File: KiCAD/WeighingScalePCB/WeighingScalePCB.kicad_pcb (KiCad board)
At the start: 4 copper layers, 83.1 x 31.9 mm, 41 parts, among them J1 Conn_01x04_Pin, Q1 MMBT2222A, Q2 BSS138, Q3 BSS138, T1 TouchPad, T2 TouchPad, U1 XIAO-ESP32-S3-SMD, U2 HX711, U3 SSD1306, U4 RT9193-33GB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

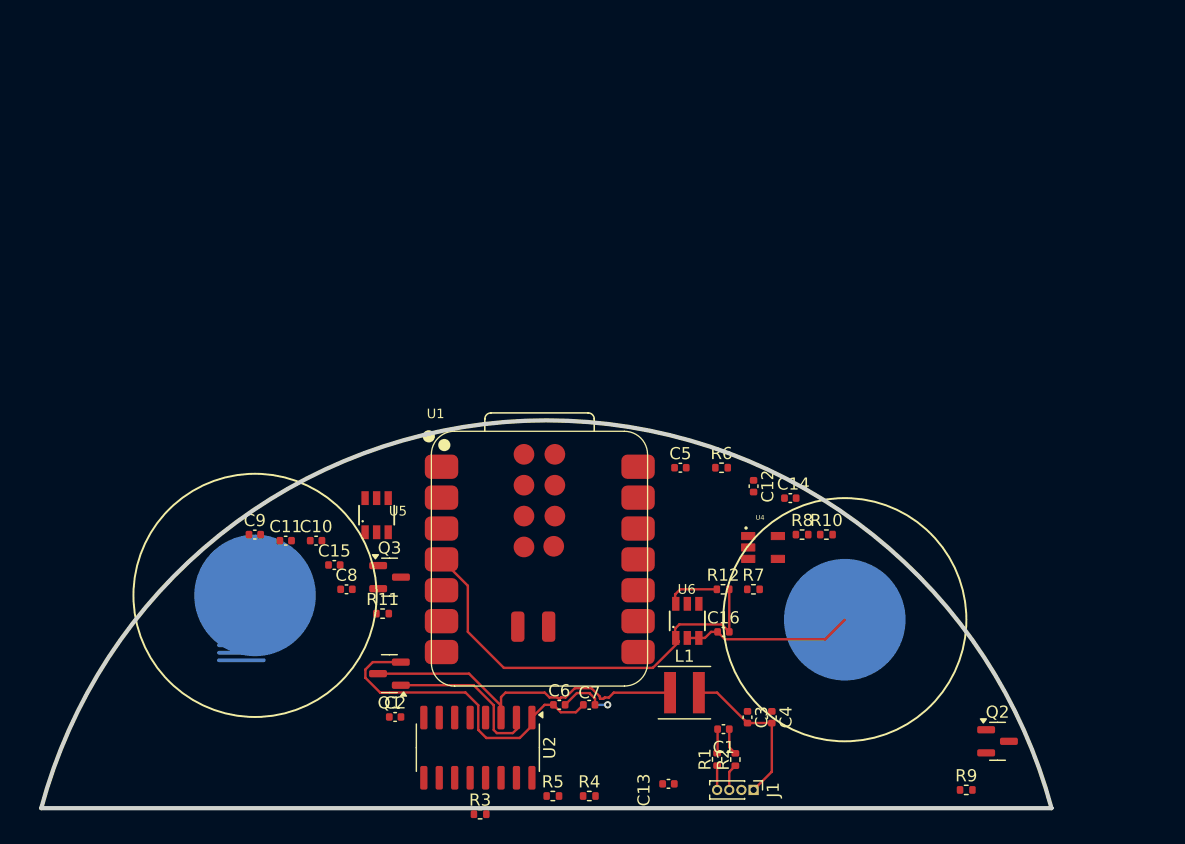
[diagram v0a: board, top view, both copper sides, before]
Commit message: imported schematic footprints to layout, noted list of missing fp
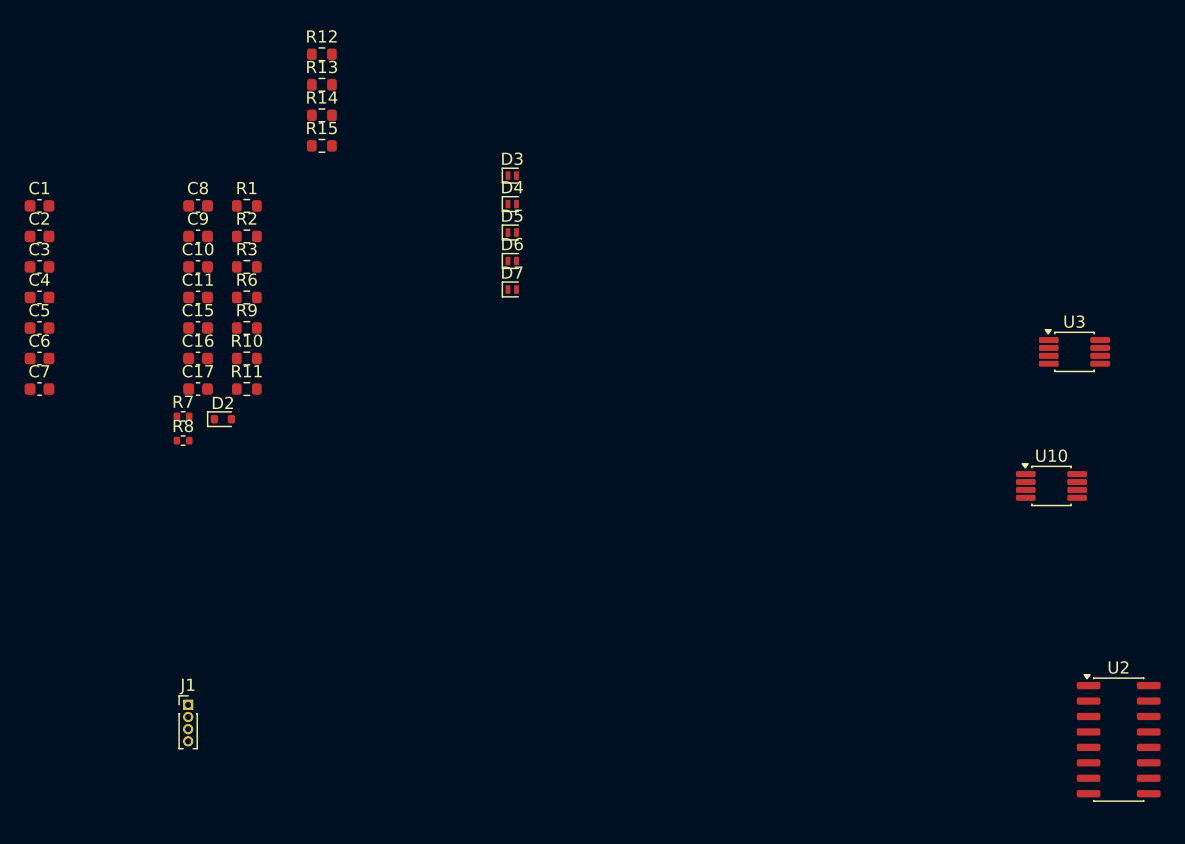
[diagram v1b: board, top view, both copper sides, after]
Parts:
- removed C12, C14: 10uF, Capacitor_SMD:C_0402_1005Metric
- removed C13: 1uF, Capacitor_SMD:C_0402_1005Metric
- removed L1: 3.3uH, Inductor_SMD:L_Coilcraft_XxL4040
- removed Q1: MMBT2222A, Package_TO_SOT_SMD:SOT-23
- removed Q2, Q3: BSS138, Package_TO_SOT_SMD:SOT-23
- removed R4, R5: 100, Resistor_SMD:R_0402_1005Metric
- removed T1, T2: TouchPad, 0my_project:Touch-Pad_10mm
- removed U1: XIAO-ESP32-S3-SMD, Seeed Studio XIAO Series Library:XIAO-ESP32C6-SMD
- removed U4: RT9193-33GB, RT9193-33GB:SOT94P279X129-5N
- removed U5, U6: TTP223-BA6, TTP223-BA6:SOT23-6
- added C17: 0.1uF, Capacitor_SMD:C_0603_1608Metric, F.Cu at (49.8, 138.5)
- added D2: 1N4148WT, Diode_SMD:D_SOD-523, F.Cu at (51.9, 141.0)
- added D3: PESD3V3U1UL, Diode_SMD:D_SOD-882, F.Cu at (75.7, 121.0)
- added D4: PESD3V3U1UL, Diode_SMD:D_SOD-882, F.Cu at (75.7, 123.3)
- added D5: PESD3V3U1UL, Diode_SMD:D_SOD-882, F.Cu at (75.7, 125.7)
- added D6: PESD3V3U1UL, Diode_SMD:D_SOD-882, F.Cu at (75.7, 128.0)
- added D7: PESD3V3U1UL, Diode_SMD:D_SOD-882, F.Cu at (75.7, 130.3)
- added R13: 10K, Resistor_SMD:R_0603_1608Metric, F.Cu at (60.0, 113.5)
- added R14: R_US, Resistor_SMD:R_0603_1608Metric, F.Cu at (60.0, 116.0)
- added R15: R_US, Resistor_SMD:R_0603_1608Metric, F.Cu at (60.0, 118.5)
- added U10: LMC555xMM, Package_SO:VSSOP-8_3x3mm_P0.65mm, F.Cu at (120.0, 146.5)
- C1, C15, C16, C2, C3, C4, C5, C6, C7: footprint Capacitor_SMD:C_0402_1005Metric -> Capacitor_SMD:C_0603_1608Metric
- C10, C8: value 1uF -> 0.1u; footprint Capacitor_SMD:C_0402_1005Metric -> Capacitor_SMD:C_0603_1608Metric
- C11: value 10uF -> 0.1u; footprint Capacitor_SMD:C_0402_1005Metric -> Capacitor_SMD:C_0603_1608Metric
- C9: value 1uF -> 1u; footprint Capacitor_SMD:C_0402_1005Metric -> Capacitor_SMD:C_0603_1608Metric
- R1, R2, R3: footprint Resistor_SMD:R_0402_1005Metric -> Resistor_SMD:R_0603_1608Metric
- R10: value 10K -> 1K; footprint Resistor_SMD:R_0402_1005Metric -> Resistor_SMD:R_0603_1608Metric
- R11: value 1K -> 200K; footprint Resistor_SMD:R_0402_1005Metric -> Resistor_SMD:R_0603_1608Metric
- R12: value 1K -> 470K; footprint Resistor_SMD:R_0402_1005Metric -> Resistor_SMD:R_0603_1608Metric
- R6: value 100 -> 200K; footprint Resistor_SMD:R_0402_1005Metric -> Resistor_SMD:R_0603_1608Metric
- R9: value 10K -> 200K; footprint Resistor_SMD:R_0402_1005Metric -> Resistor_SMD:R_0603_1608Metric
- U3: value SSD1306 -> LMC555xMM; footprint KiCad-SSD1306_OLED-0.91-128x32-master:SSD1306_OLED-0.91-128x32 -> Package_SO:VSSOP-8_3x3mm_P0.65mm; moved to F.Cu
- moved C1 70.8 mm to (36.8, 123.5), turned to 0 degrees
- moved R9 70.3 mm to (53.8, 133.5)
- moved C4 69.4 mm to (36.8, 131.0), turned to 0 degrees
- moved C3 69.0 mm to (36.8, 128.5), turned to 0 degrees
- moved R1 59.7 mm to (53.8, 123.5), turned to 0 degrees
- moved R2 58.9 mm to (53.8, 126.0), turned to 0 degrees
- moved R12 55.0 mm to (60.0, 111.0)
- moved C5 53.9 mm to (36.8, 133.5)
- moved U2 52.7 mm to (125.5, 167.4), turned to 0 degrees
- moved C7 52.1 mm to (36.8, 138.5)
- moved R8 51.5 mm to (48.6, 142.8)
- moved C6 51.4 mm to (36.8, 136.0)
- moved R10 49.8 mm to (53.8, 136.0)
- moved C2 49.2 mm to (36.8, 126.0)
- moved R7 49.0 mm to (48.6, 140.8)
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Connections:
- C10 pad 1: GND -> /trigg
- C10 pad 2: VCC -> Net-(U10-GND)
- C11 pad 1: GND -> Net-(U10-CV)
- C11 pad 2: Net-(U3-VCC) -> Net-(U10-GND)
- C8 pad 1: Net-(U3-C2N) -> Net-(U3-CV)
- C8 pad 2: Net-(U3-C2P) -> GND
- C9 pad 1: Net-(U3-C1N) -> Net-(U3-DIS)
- C9 pad 2: Net-(U3-C1P) -> GND
- R10 pad 1: VCC -> Net-(IC2-VOUT)
- R10 pad 2: SDA_5V -> GND
- R11 pad 1: VCC -> /V_BAT
- R11 pad 2: GND -> Net-(Q2-D)
- R12 pad 2: GND -> Net-(U3-DIS)
- R3 pad 1: Net-(JP1-B) -> Net-(JP3-A)
- R6 pad 1: Net-(U3-IREF) -> /V_BAT
- R6 pad 2: GND -> Net-(U1-GPIO0_A0_D0)
- R7 pad 1: 3.3V -> VCC
- R7 pad 2: SCL_3.3V -> SCL
- R8 pad 1: 3.3V -> VCC
- R8 pad 2: SDA_3.3V -> SDA
- R9 pad 1: VCC -> Net-(U1-GPIO0_A0_D0)
- R9 pad 2: SCL_5V -> GND
- U2 pad 15: Net-(JP1-B) -> Net-(JP3-B)
- U2 pad 2: Net-(Q1-B) -> unconnected-(U2-BASE-Pad2)
- U2 pad 3: Net-(Q1-C) -> Net-(J1-Pin_1)
- U2 pad 4: Net-(U2-VFB) -> GND
- U3 pad 1: Net-(U3-C2P) -> GND
- U3 pad 2: Net-(U3-C2N) -> Net-(Q4-D)
- U3 pad 3: Net-(U3-C1P) -> Net-(D5-K)
- U3 pad 4: Net-(U3-C1N) -> Net-(U3-R)
- U3 pad 5: VCC -> Net-(U3-CV)
- U3 pad 6: unconnected-(U3-NC-Pad6) -> Net-(U3-DIS)
- U3 pad 7: GND -> Net-(U3-DIS)
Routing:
- net VCC: track 31.4 -> 0.00 mm
- net Net-(Q1-C): track 29.1 -> 0.00 mm
- net Time: track 26.4 -> 0.00 mm
- net GND: track 14.7 -> 0.00 mm
- net Net-(D4-K): track 14.1 -> 0.00 mm
- net Net-(Q1-B): track 13.4 -> 0.00 mm
- net Net-(J1-Pin_1): track 13.2 -> 0.00 mm
- net Net-(U2-INA+): track 2.20 -> 0.00 mm
- net Net-(J1-Pin_3): track 2.20 -> 0.00 mm
- net Net-(U2-INA-): track 2.00 -> 0.00 mm
- net (no net): track 1.00 -> 0.00 mm, vias 1 -> 0
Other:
- board outline removed

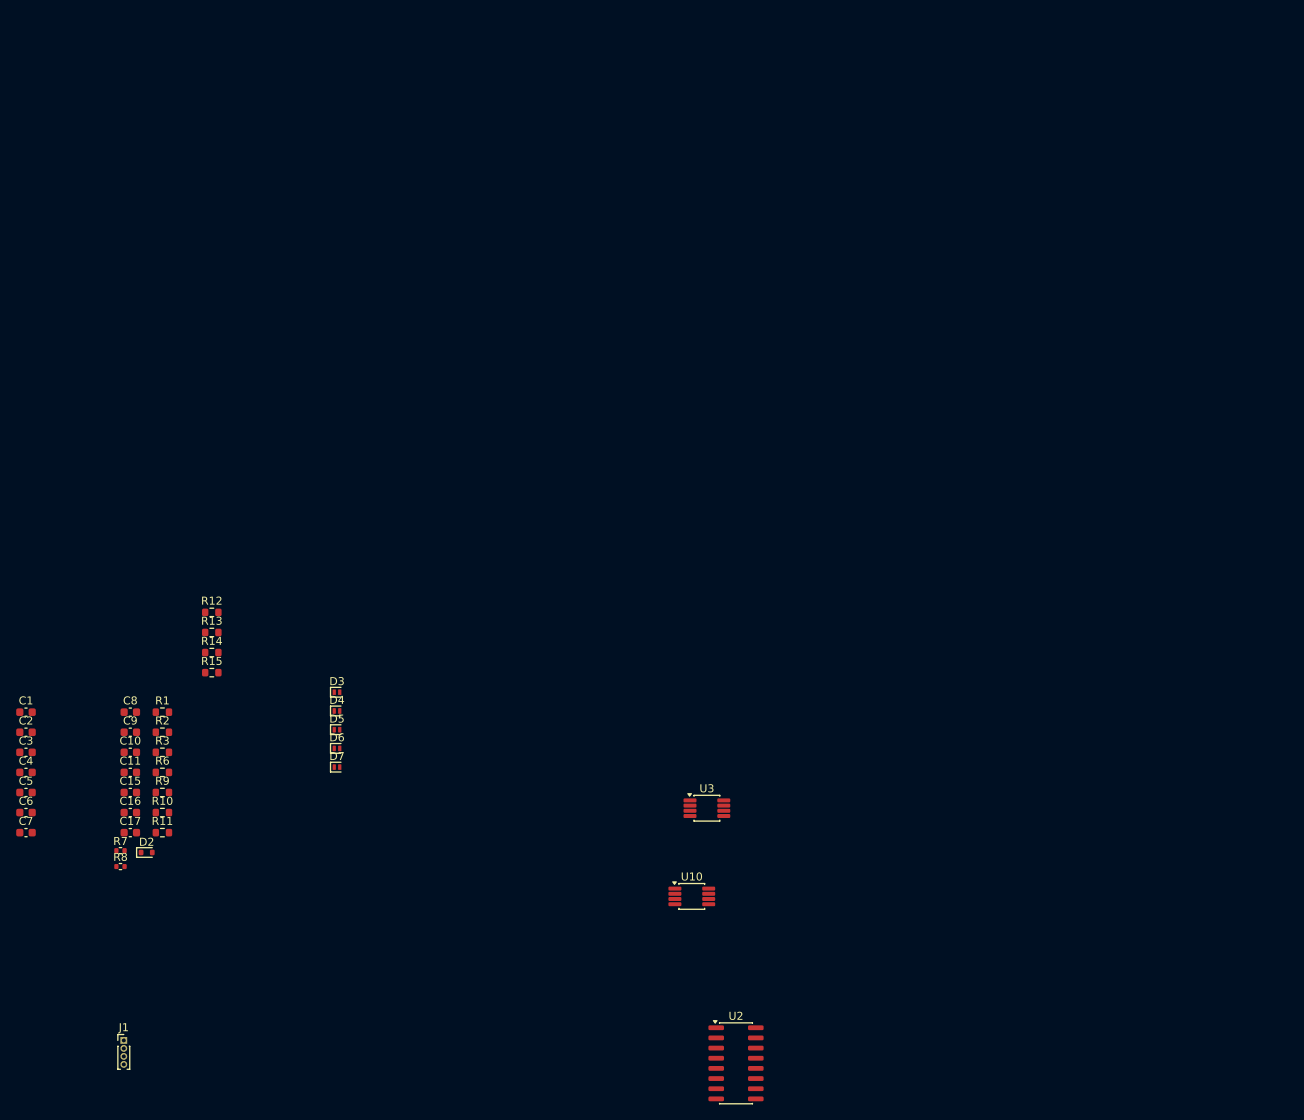
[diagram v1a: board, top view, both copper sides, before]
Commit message: Added flowchart for board and dxf in the layout for card edge and placement of components
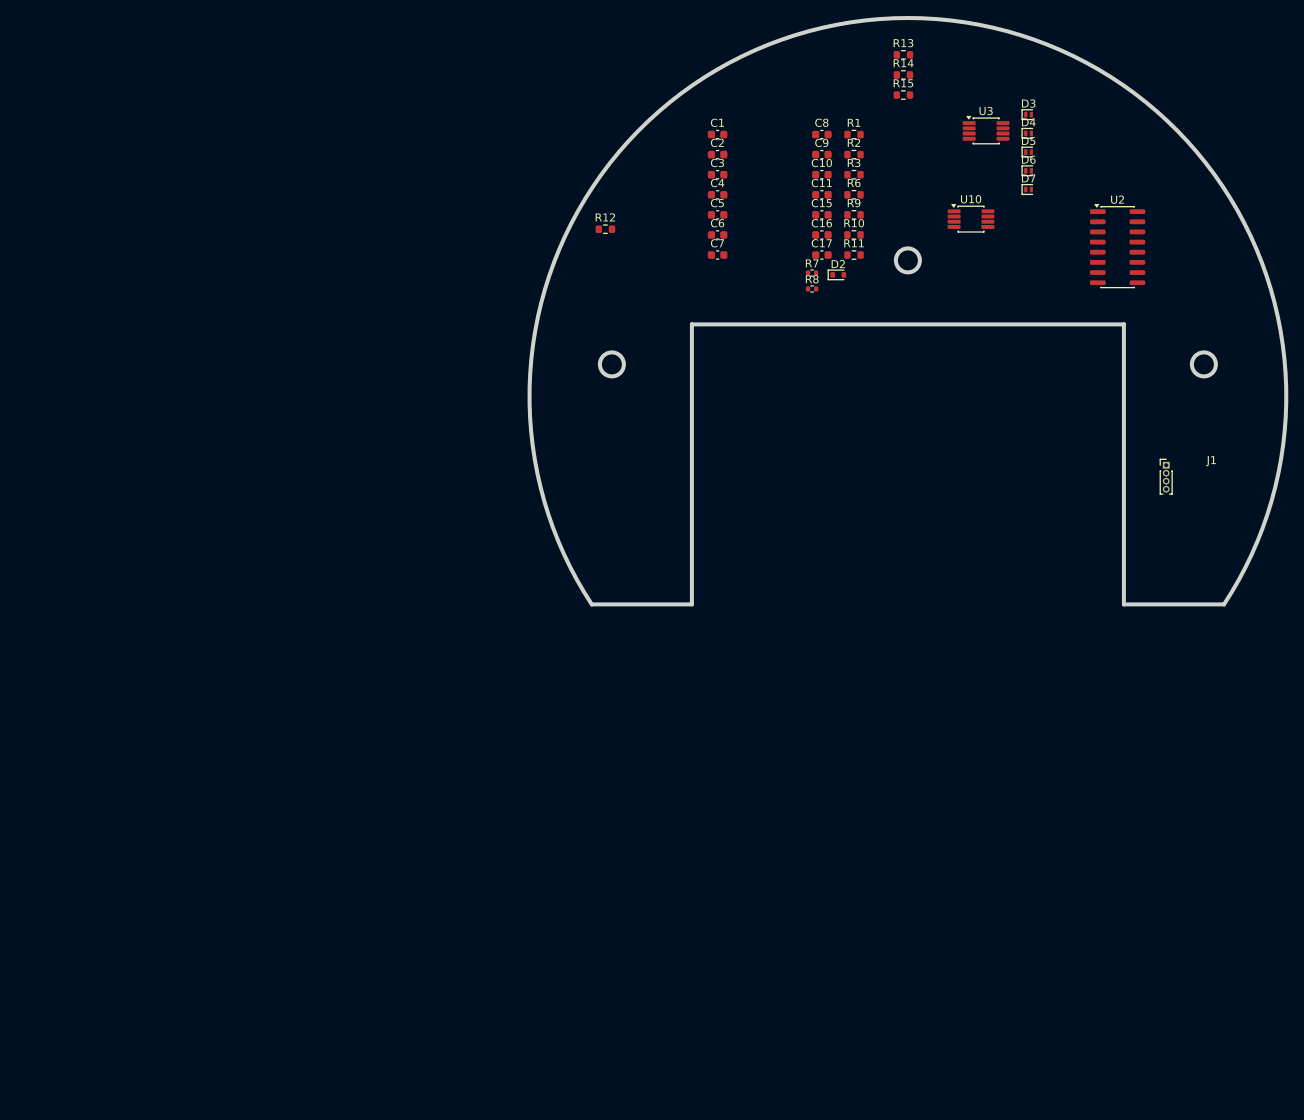
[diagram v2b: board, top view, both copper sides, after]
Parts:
- moved J1 148.8 mm to (179.3, 92.6)
- moved R10 112.6 mm to (140.3, 63.8)
- moved R3 112.6 mm to (140.3, 56.3)
- moved C10 112.6 mm to (136.3, 56.3)
- moved C11 112.6 mm to (136.3, 58.8)
- moved C16 112.6 mm to (136.3, 63.8)
- moved C17 112.6 mm to (136.3, 66.3)
- moved C2 112.6 mm to (123.2, 53.8)
- moved C3 112.6 mm to (123.2, 56.3)
- moved C4 112.6 mm to (123.2, 58.8)
- moved C6 112.6 mm to (123.2, 63.8)
- moved C7 112.6 mm to (123.2, 66.3)
- moved C9 112.6 mm to (136.3, 53.8)
- moved D2 112.6 mm to (138.3, 68.8)
- moved D3 112.6 mm to (162.1, 48.8)
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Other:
- board outline added: 94.6 x 73.3 mm
- board text added: "Overlay user.4 layer on board edge while doing component placement"

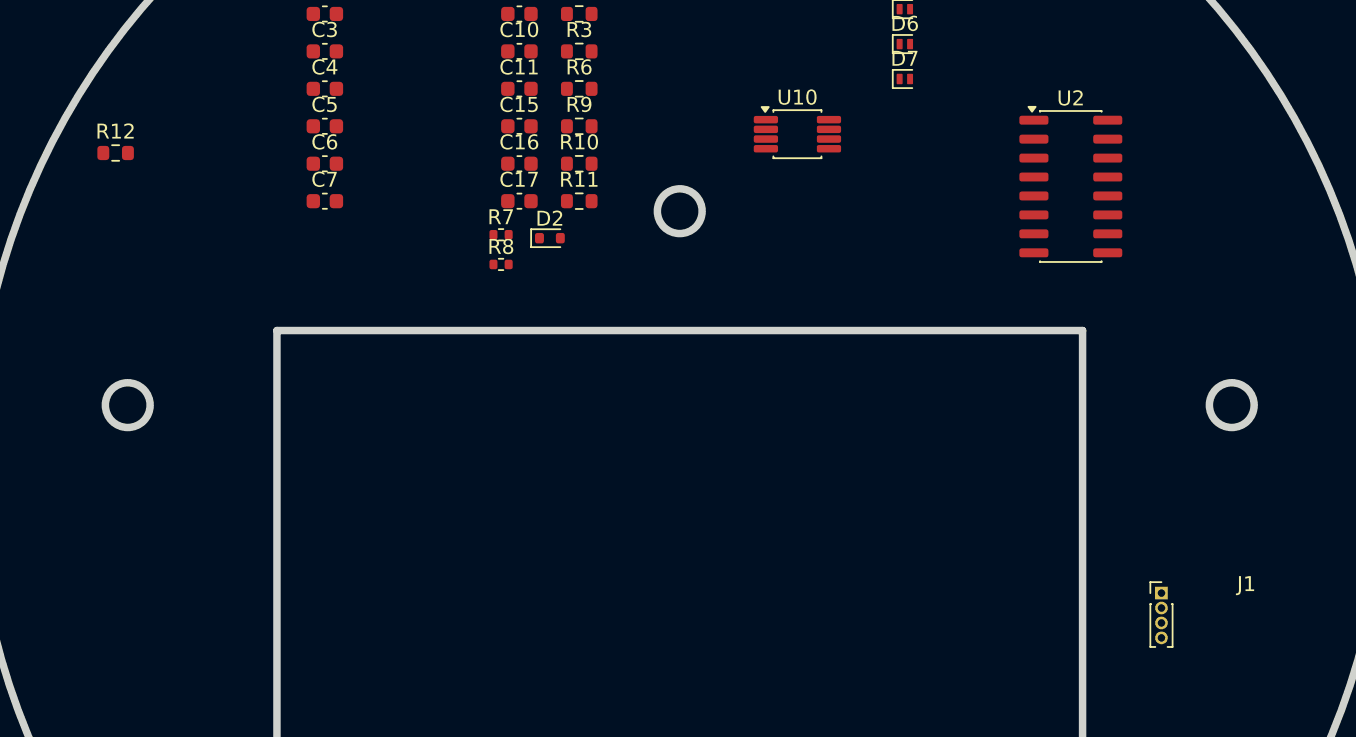
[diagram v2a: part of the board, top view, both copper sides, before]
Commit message: Corrected time and tare orring circuit
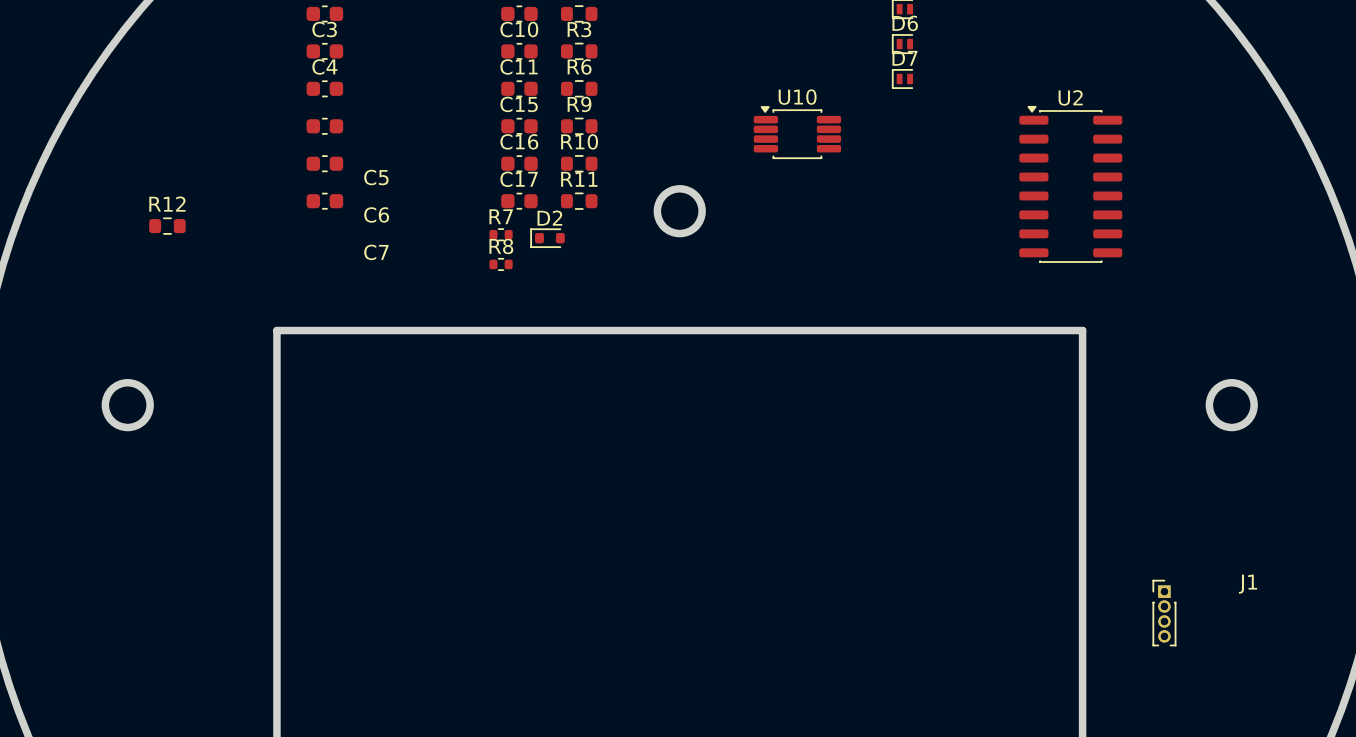
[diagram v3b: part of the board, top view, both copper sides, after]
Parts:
- moved R12 6.01 mm to (112.7, 68.0)
- moved J1 0.22 mm to (179.5, 92.5)
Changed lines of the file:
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@@
 		)
 		(fp_text user "${REFERENCE}"
-			(at 0 0 0)
+			(at 3.475 4.9 0)
 			(layer "F.Fab")
 			(effects
@@
 	(footprint "Connector_PinHeader_1.00mm:PinHeader_1x04_P1.00mm_Vertical"
 		(layer "F.Cu")
-		(at 179.3 92.6)
+		(at 179.5 92.5)
 		(descr "Through hole straight pin header, 1x04, 1.00mm pitch, single row")
 		(tags "Through hole pin header THT 1x04 1.00mm single row")
@@
 		(tags "capacitor")
 		(property "Reference" "C6"
-			(at 0 -1.43 0)
+			(at 3.475 3.47 0)
 			(layer "F.SilkS")
 			(effects
@@
 		)
 		(fp_text user "${REFERENCE}"
-			(at 0 0 0)
+			(at 3.475 4.9 0)
 			(layer "F.Fab")
 			(effects
@@
 		(tags "capacitor")
 		(property "Reference" "C5"
-			(at 0 -1.43 0)
+			(at 3.475 3.47 0)
 			(layer "F.SilkS")
 			(effects
@@
 		)
 		(fp_text user "${REFERENCE}"
-			(at 0 0 0)
+			(at 3.475 4.9 0)
 			(layer "F.Fab")
 			(effects
@@
 		(tags "capacitor")
 		(property "Reference" "C7"
-			(at 0 -1.43 0)
+			(at 3.475 3.47 0)
 			(layer "F.SilkS")
 			(effects
@@
 		)
 		(fp_text user "${REFERENCE}"
-			(at 0 0 0)
+			(at 3.475 4.9 0)
 			(layer "F.Fab")
 			(effects
@@
 	(footprint "Resistor_SMD:R_0603_1608Metric"
 		(layer "F.Cu")
-		(at 109.2 63.1)
+		(at 112.675 68)
 		(descr "Resistor SMD 0603 (1608 Metric), square (rectangular) end terminal, IPC-7351 nominal, (Body size source: IPC-SM-782 page 72, https://www.pcb-3d.com/wordpress/wp-content/uploads/ipc-sm-782a_amendment_1_and_2.pdf), generated with kicad-footprint-generator")
 		(tags "resistor")
